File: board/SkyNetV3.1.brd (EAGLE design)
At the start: 23.9 x 59 mm, 48 parts, among them IC2 RF4463PRO, IC3 LPC1769, IC4 BCX17, Q1 32.768KHz, Q2 12MHz, U1 MCP16301T-I/CHY, X2 CONN-SMATHD

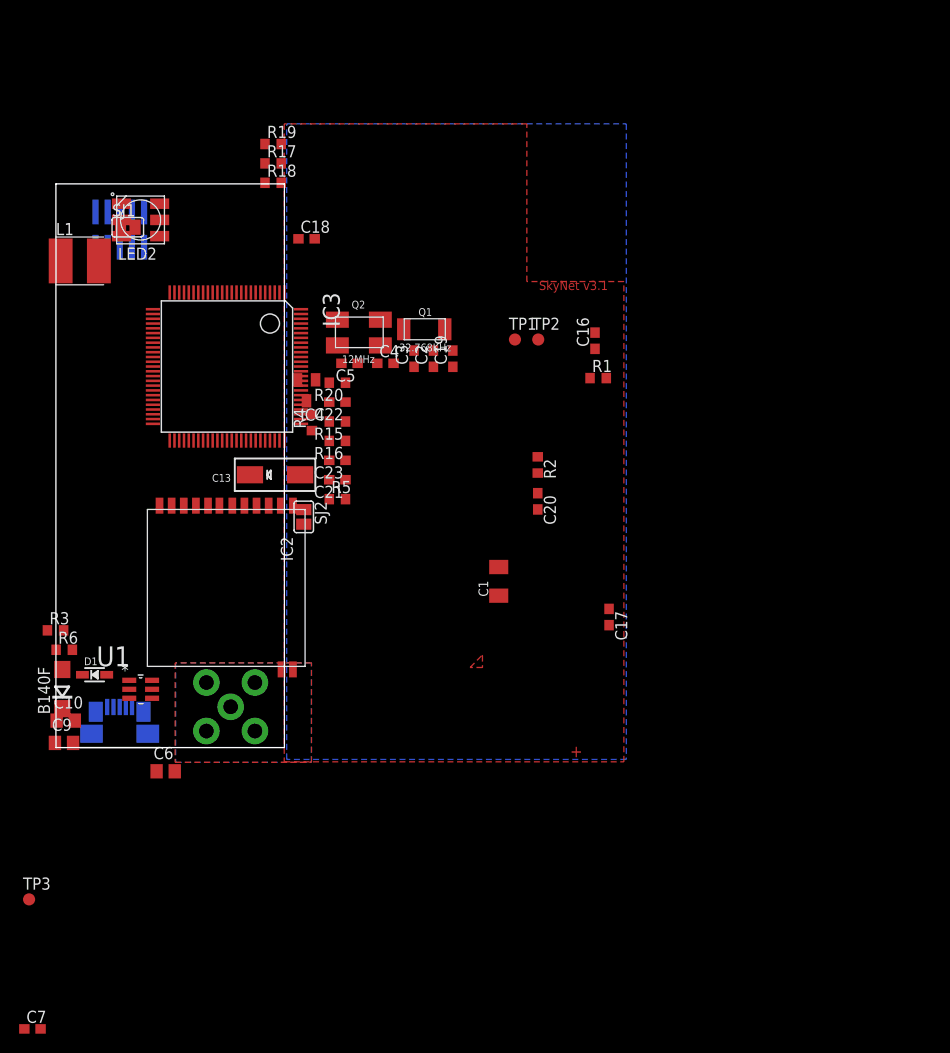
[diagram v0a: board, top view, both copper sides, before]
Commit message: improved placement
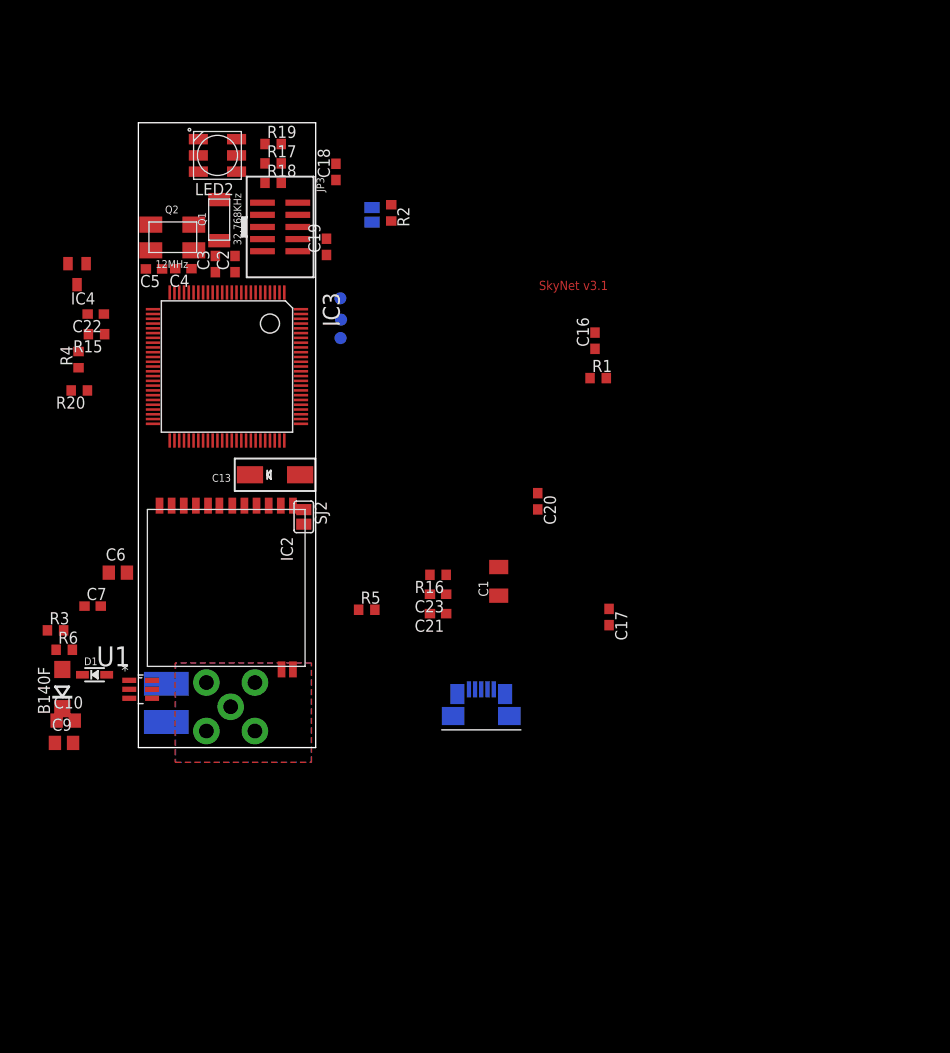
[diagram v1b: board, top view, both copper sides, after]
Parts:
- moved TP3 67.2 mm to (31.8, 46.4), flipped to the bottom
- moved L1 47.2 mm to (13.6, 8.18), flipped to the bottom, turned to 270 degrees
- moved C7 44.7 mm to (5.87, 18.3)
- moved USB1 37.9 mm to (46.6, 6.80)
- moved R2 30.5 mm to (37.1, 59.5)
- moved R20 27.0 mm to (4.47, 40.9)
- moved IC4 26.9 mm to (4.24, 53.1)
- moved C22 26.9 mm to (6.20, 48.9)
- moved R15 26.8 mm to (6.27, 46.8)
- moved SJ1 25.6 mm to (35.1, 59.3), flipped to the bottom, turned to 270 degrees
- moved R4 25.3 mm to (4.39, 44.1)
- moved Q1 24.4 mm to (19.2, 58.8), turned to 90 degrees
- moved C4 23.4 mm to (15.4, 53.6), turned to 180 degrees
- moved C3 23.0 mm to (18.7, 54.1)
- moved C2 23.0 mm to (20.8, 54.1)
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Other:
- board size 23.9 x 59 mm -> 18.6 x 65.4 mm
- board text removed: "+"

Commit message: improved placement
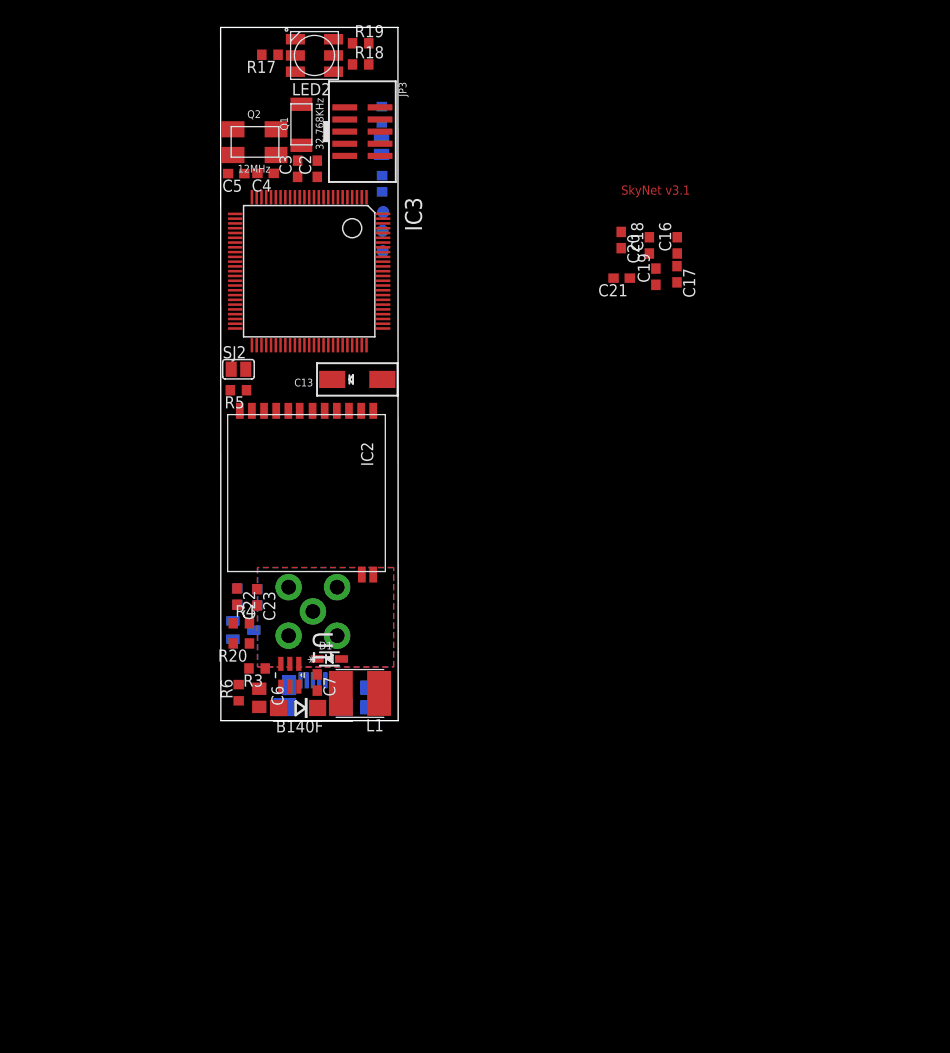
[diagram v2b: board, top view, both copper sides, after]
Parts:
- removed C1: 100n, rcl:C1206K
- C7: value (none) -> 100n
- moved IC4 41.1 mm to (21.7, 15.8), flipped to the bottom, turned to 90 degrees
- moved C21 40.0 mm to (61.3, 52.7)
- moved C17 36.6 mm to (67.1, 53.1)
- moved C19 34.6 mm to (64.8, 52.8)
- moved C18 33.7 mm to (64.2, 56.1)
- moved C9 33.1 mm to (35.5, 9.78), flipped to the bottom
- moved C22 33.1 mm to (21.0, 19.3), turned to 270 degrees
- moved C10 32.5 mm to (35.5, 7.72), flipped to the bottom
- moved R4 32.4 mm to (21.4, 16.5), turned to 0 degrees
- moved R20 31.5 mm to (21.4, 14.4)
- moved R15 31.2 mm to (21.0, 19.3), flipped to the bottom, turned to 270 degrees
- moved R1 30.4 mm to (36.2, 62.5), flipped to the bottom, turned to 90 degrees
- moved C20 28.7 mm to (61.2, 56.6)
- moved R5 26.6 mm to (21.1, 40.9), turned to 180 degrees
- moved C7 24.8 mm to (29.4, 10.3), turned to 270 degrees
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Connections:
- net +3V3: no longer C1.1
- net GND: no longer C1.2
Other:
- board size 18.6 x 65.4 mm -> 18.6 x 72.6 mm

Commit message: almost done
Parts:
- removed C9: 10u, rcl:C0805
- removed SJ1: RESET, jumper:SJ
- removed USB1: MOLEX-47346-0001, usb_con-update:MOLEX-47364-0001
- added JP1: (no value), jumper:JP1
- added TP4, TP5: PTR1B1,27, testpad:B1,27
- added TP6: PTR1B2,54, testpad:B2,54
- moved C17 47.1 mm to (24.3, 33.1), flipped to the bottom, turned to 0 degrees
- moved C6 45.4 mm to (23.2, 54.1), turned to 180 degrees
- moved R6 43.1 mm to (29.5, 51.5), turned to 270 degrees
- moved B140F 42.7 mm to (22.7, 50.1), turned to 90 degrees
- moved C16 42.5 mm to (31.4, 33.1), flipped to the bottom, turned to 180 degrees
- moved C21 42.2 mm to (20.6, 41.5), turned to 270 degrees
- moved C20 41.5 mm to (20.6, 48.2), turned to 90 degrees
- moved C19 40.9 mm to (24.3, 58.2)
- moved U1 40.1 mm to (26.1, 51.2), turned to 180 degrees
- moved C7 38.0 mm to (26.1, 48.2), turned to 180 degrees
- moved R3 37.3 mm to (29.4, 48.5), turned to 270 degrees
- moved C10 37.0 mm to (33.5, 44.7), flipped to the top
- moved R4 36.3 mm to (32.2, 51.2), turned to 270 degrees
- moved L1 35.8 mm to (24.4, 43.7), turned to 90 degrees
- moved R15 35.3 mm to (36.2, 51.2), flipped to the top, turned to 90 degrees
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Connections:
- net +3V3: now also TP6.TP; no longer C9.1
- net +5V: now also JP1.2; no longer USB1.1
- net GND: now also JP1.1; no longer C9.2, SJ1.1, USB1.5, USB1.GND1, USB1.GND2, USB1.GND3, USB1.GND4
- net RESET: no longer SJ1.2
- net USB-CABLE-D+: now also TP5.TP; no longer USB1.3
- net USB-CABLE-D-: now also TP4.TP; no longer USB1.2
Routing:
- net GND: track 0.00 -> 154.5 mm, vias 0 -> 12
- net +3V3: track 0.00 -> 111.4 mm, vias 0 -> 6
- net USB-CON: track 0.00 -> 16.9 mm, vias 0 -> 3
- net RESET: track 0.00 -> 15.7 mm, vias 0 -> 1
- net JTAG_TDI: track 0.00 -> 13.9 mm, vias 0 -> 1
- net JTAG_TDO: track 0.00 -> 13.6 mm, vias 0 -> 1
- net RTCX1: track 0.00 -> 12.5 mm
- net JTAG_TCK: track 0.00 -> 11.0 mm, vias 0 -> 1
- net JTAG_TMS: track 0.00 -> 10.7 mm, vias 0 -> 1
- net XTAL2: track 0.00 -> 10.6 mm
- net RF-NIRQ: track 0.00 -> 10.4 mm, vias 0 -> 1
- net N$1: track 0.00 -> 9.54 mm
- net +5V: track 0.00 -> 8.78 mm
- net USB-CABLE-D+: track 0.00 -> 8.78 mm, vias 0 -> 1
- net RTCX2: track 0.00 -> 8.59 mm
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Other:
- board size 18.6 x 72.6 mm -> 18.6 x 46.9 mm
- board text added: "masse schleife 1x rum"
- board text added: "todo: led i2c(46 47) gpios (75)"

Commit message: mitten drin
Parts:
- added TP10, TP11, TP12, TP13, TP7, TP8, TP9: PTR1B1,27, testpad:B1,27
- TP3: value PTR1B1,27 -> PTR1B2,54; device testpad:B1,27 -> testpad:B2,54
- moved SJ2 3.96 mm to (36.5, 26.7)
- moved TP3 2.14 mm to (21.3, 22.9)
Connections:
- new net N$10: IC3.50, TP13.TP
- new net N$3: IC3.75, TP8.TP
- new net N$5: IC3.76, TP9.TP
- new net N$6: IC3.77, TP10.TP
- new net N$7: IC3.74, TP7.TP
- new net N$8: IC3.49, TP12.TP
- new net N$9: IC3.48, TP11.TP
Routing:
- net PROG: track 5.80 -> 9.76 mm
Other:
- board text added: "led??"
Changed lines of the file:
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@@
 <text x="46.101" y="39.2684" size="1.778" layer="1">todo: led i2c(46 47) gpios (75)</text>
 <text x="46.0756" y="36.0426" size="1.778" layer="1">masse schleife 1x rum</text>
+<text x="40.7416" y="32.2834" size="1.778" layer="1">led??</text>
 </plain>
 <attributes>
@@
 <element name="C17" library="rcl" package="C0603" value="100n" x="24.3332" y="33.1216" rot="MR0"/>
 <element name="LED2" library="adafruit" package="RGBLED5050" value="RGBLED5050" x="46.8886" y="55.83825" rot="R270"/>
-<element name="SJ2" library="jumper" package="SJ" value="PROG" x="36.4848" y="30.6894" rot="MR90"/>
+<element name="SJ2" library="jumper" package="SJ" value="PROG" x="36.5356" y="26.727" rot="MR90"/>
 <element name="C13" library="microbuilder" package="EIA6032-28/C-W" value="100u" x="33.0712" y="41.81935" rot="R180"/>
 <element name="X2" library="SteveMarple" package="SMA-THD" value="CONN-SMATHD" x="28.9306" y="17.7546" rot="MR0"/>
@@
 <element name="C6" library="rcl" package="C0805" value="10u" x="23.2156" y="54.102" rot="R180"/>
 <element name="JP3" library="microbuilder" package="2X05_1.27MM_SMT" value="JTAG" x="30.4038" y="56.5912"/>
-<element name="TP3" library="testpad" package="B1,27" value="PTR1B1,27" x="20.6502" y="24.9428" rot="MR0">
-<attribute name="TP_SIGNAL_NAME" value="" x="20.6502" y="24.9428" size="1.778" layer="28" rot="MR0" display="off"/>
-</element>
 <element name="U1" library="skynet_other" package="SOT95P290X145-6N" value="MCP16301T-I/CHY" x="26.1112" y="51.1556" rot="R180">
 <attribute name="PACKAGE" value="SOT23-6" x="26.1112" y="51.1556" size="1.778" layer="27" rot="R180" display="off"/>
@@
 <element name="TP6" library="testpad" package="B2,54" value="PTR1B2,54" x="27.8892" y="42.0624">
 <attribute name="TP_SIGNAL_NAME" value="" x="27.8892" y="42.0624" size="1.778" layer="27" display="off"/>
+</element>
+<element name="TP7" library="testpad" package="B1,27" value="PTR1B1,27" x="20.8788" y="26.8224" rot="MR0">
+<attribute name="TP_SIGNAL_NAME" value="" x="20.8788" y="26.8224" size="1.778" layer="28" rot="MR0" display="off"/>
+</element>
+<element name="TP8" library="testpad" package="B1,27" value="PTR1B1,27" x="20.9296" y="29.1592" rot="MR0">
+<attribute name="TP_SIGNAL_NAME" value="" x="20.9296" y="29.1592" size="1.778" layer="28" rot="MR0" display="off"/>
+</element>
+<element name="TP9" library="testpad" package="B1,27" value="PTR1B1,27" x="20.9804" y="33.782" rot="MR0">
+<attribute name="TP_SIGNAL_NAME" value="" x="20.9804" y="33.782" size="1.778" layer="28" rot="MR0" display="off"/>
+</element>
+<element name="TP10" library="testpad" package="B1,27" value="PTR1B1,27" x="20.7518" y="31.7246" rot="MR0">
+<attribute name="TP_SIGNAL_NAME" value="" x="20.7518" y="31.7246" size="1.778" layer="28" rot="MR0" display="off"/>
+</element>
+<element name="TP11" library="testpad" package="B1,27" value="PTR1B1,27" x="36.449" y="30.099" rot="MR0">
+<attribute name="TP_SIGNAL_NAME" value="" x="36.449" y="30.099" size="1.778" layer="28" rot="MR0" display="off"/>
+</element>
+<element name="TP12" library="testpad" package="B1,27" value="PTR1B1,27" x="36.4998" y="32.2834" rot="MR0">
+<attribute name="TP_SIGNAL_NAME" value="" x="36.4998" y="32.2834" size="1.778" layer="28" rot="MR0" display="off"/>
+</element>
+<element name="TP3" library="testpad" package="B2,54" value="PTR1B2,54" x="21.3106" y="22.9108" rot="MR0">
+<attribute name="TP_SIGNAL_NAME" value="" x="21.3106" y="22.9108" size="1.778" layer="28" rot="MR0" display="off"/>
+</element>
+<element name="TP13" library="testpad" package="B1,27" value="PTR1B1,27" x="6.6802" y="9.144">
+<attribute name="TP_SIGNAL_NAME" value="" x="6.6802" y="9.144" size="1.778" layer="27" display="off"/>
 </element>
 </elements>
@@
 <contactref element="JP3" pad="5"/>
 <contactref element="JP3" pad="9"/>
-<contactref element="TP3" pad="TP"/>
 <contactref element="U1" pad="2"/>
 <contactref element="B140F" pad="A"/>
@@
 <wire x1="25.0952" y1="57.4294" x2="23.495" y2="55.8292" width="0.1524" layer="16"/>
 <wire x1="23.495" y1="55.8292" x2="21.4122" y2="55.8292" width="0.1524" layer="16"/>
+<contactref element="TP3" pad="TP"/>
 <wire x1="36.3286" y1="46.8488" x2="42.6584" y2="50.2666" width="0" layer="19" extent="1-16"/>
-<wire x1="36.4848" y1="29.9274" x2="35.2486" y2="29.9146" width="0" layer="19" extent="1-16"/>
-<wire x1="20.6502" y1="24.9428" x2="22.5298" y2="28.6004" width="0" layer="19" extent="1-16"/>
+<wire x1="36.5356" y1="25.965" x2="35.2486" y2="29.9146" width="0" layer="19" extent="1-16"/>
 <wire x1="34.057975" y1="21.615975" x2="33.9344" y2="28.6004" width="0" layer="19" extent="1-1"/>
+<wire x1="31.4706" y1="20.2946" x2="34.057975" y2="21.615975" width="0" layer="19" extent="1-1"/>
+<wire x1="26.3906" y1="20.2946" x2="31.4706" y2="20.2946" width="0" layer="19" extent="1-1"/>
+<wire x1="31.4706" y1="15.2146" x2="31.4706" y2="20.2946" width="0" layer="19" extent="1-1"/>
+<wire x1="26.3906" y1="15.2146" x2="26.3906" y2="20.2946" width="0" layer="19" extent="1-1"/>
+<wire x1="21.3106" y1="22.9108" x2="26.3906" y2="15.2146" width="0" layer="19" extent="1-1"/>
 </signal>
 <signal name="RTCX1">
@@
 <wire x1="35.2044" y1="33.108" x2="35.2162" y2="33.0962" width="0.1524" layer="16"/>
 <wire x1="35.2162" y1="33.0962" x2="36.4848" y2="31.8276" width="0.1524" layer="16"/>
-<wire x1="36.4848" y1="31.8276" x2="36.4848" y2="31.4514" width="0.1524" layer="16"/>
+<wire x1="36.4848" y1="31.8276" x2="36.5356" y2="27.489" width="0.1524" layer="16"/>
 </signal>
 <signal name="RESET">
@@
 <wire x1="28.1432" y1="52.0954" x2="27.305" y2="52.0954" width="0.1524" layer="1"/>
 </signal>
+<signal name="N$3">
+<contactref element="IC3" pad="75"/>
+<contactref element="TP8" pad="TP"/>
+<wire x1="20.9296" y1="29.1592" x2="22.5786" y2="35.5988" width="0" layer="19" extent="1-16"/>
+</signal>
+<signal name="N$5">
+<contactref element="IC3" pad="76"/>
+<contactref element="TP9" pad="TP"/>
+<wire x1="20.9804" y1="33.782" x2="20.8286" y2="37.3488" width="0" layer="19" extent="1-16"/>
+</signal>
+<signal name="N$6">
+<contactref element="IC3" pad="77"/>
+<contactref element="TP10" pad="TP"/>
+<wire x1="20.7518" y1="31.7246" x2="20.8286" y2="37.8488" width="0" layer="19" extent="1-16"/>
+</signal>
+<signal name="N$7">
+<contactref element="IC3" pad="74"/>
+<contactref element="TP7" pad="TP"/>
+<wire x1="20.8788" y1="26.8224" x2="23.0786" y2="35.5988" width="0" layer="19" extent="1-16"/>
+</signal>
+<signal name="N$8">
+<contactref element="IC3" pad="49"/>
+<contactref element="TP12" pad="TP"/>
+<wire x1="36.4998" y1="32.2834" x2="36.3286" y2="37.8488" width="0" layer="19" extent="16-16"/>
+</signal>
+<signal name="N$9">
+<contactref element="IC3" pad="48"/>
+<contactref element="TP11" pad="TP"/>
+<wire x1="36.449" y1="30.099" x2="36.3286" y2="38.3488" width="0" layer="19" extent="16-16"/>
+</signal>
+<signal name="N$10">
+<contactref element="IC3" pad="50"/>
+<contactref element="TP13" pad="TP"/>
+<wire x1="6.6802" y1="9.144" x2="36.3286" y2="37.3488" width="0" layer="19" extent="1-16"/>
+</signal>
 </signals>

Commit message: done
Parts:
- removed C18: 100n, rcl:C0603
- removed LED2: RGBLED5050, adafruit:RGBLED5050
- removed R18, R19: 68, rcl:R0603
- added LED1: (no value), led:CHIP-LED0805
- R17: value 100 -> 360
- moved TP13 39.0 mm to (36.4, 34.3), flipped to the bottom
- moved R17 32.9 mm to (33.4, 31.1), turned to 0 degrees
- moved TP7 1.51 mm to (20.7, 28.3)
- moved TP3 1.37 mm to (21.4, 24.3)
- moved TP8 1.17 mm to (20.7, 30.3)
- moved C16 1.02 mm to (30.4, 33.1)
- moved R5 1.02 mm to (33.4, 33.1)
- moved SJ2 0.94 mm to (35.7, 26.3), turned to 180 degrees
- moved TP9 0.61 mm to (20.7, 34.3)
- moved TP10 0.59 mm to (20.7, 32.3)
- moved X2 0.25 mm to (28.7, 17.8)
- moved TP11 0.20 mm to (36.4, 30.3)
- moved TP12 0.08 mm to (36.4, 32.3)
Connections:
- removed net LED-B: IC3.32, LED2.4
- removed net LED-B-R: LED2.3, R19.1
- removed net LED-G: IC3.35, LED2.6
- removed net LED-G-R: LED2.1, R18.1
- removed net LED-R: IC3.34, LED2.5
- new net LED: IC3.35, LED1.C
- net +3V3: no longer C18.1, R18.2, R19.2
- net GND: no longer C18.2
- net LED-R-R: now also LED1.A; no longer LED2.2
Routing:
- net LED: track 0.00 -> 20.6 mm, vias 0 -> 2
- net GND: track 154.5 -> 171.3 mm, vias 12 -> 46
- net N$9: track 0.00 -> 9.84 mm
- net ANT: track 0.00 -> 8.64 mm
- net N$7: track 0.00 -> 8.46 mm
- net N$6: track 0.00 -> 7.21 mm
- net N$8: track 0.00 -> 6.92 mm
- net N$3: track 0.00 -> 6.07 mm
- net N$5: track 0.00 -> 3.10 mm
- net N$10: track 0.00 -> 3.08 mm
- net LED-R-R: track 0.00 -> 2.63 mm
- net +3V3: track 111.4 -> 113.4 mm
- net PROG: track 9.76 -> 10.5 mm
- net RF-NIRQ: track 10.4 -> 11.0 mm
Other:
- board size 18.6 x 46.9 mm -> 19.9 x 47.4 mm
- board text added: "+5V"
- board text added: "-"
- board text added: "D+"
- board text added: "D-"
- board text added: "GND"
- board text added: "P0_8"
- board text added: "P0_9"
- board text added: "P2_0"
- board text added: "P2_1"
- board text added: "P2_13"
- board text added: "Prog"
- board text added: "RX0"
- board text added: "SCL2"
- board text added: "SDA2"
- board text added: "SkyNet v3.1 i7"
- board text added: "TX0"
- board text removed: "SkyNet v3.1"
- board text removed: "led??"
- board text removed: "masse schleife 1x rum"
- board text removed: "todo: led i2c(46 47) gpios (75)"
